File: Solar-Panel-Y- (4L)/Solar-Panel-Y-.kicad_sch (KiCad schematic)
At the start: 61 parts, among them J1 FTS-107-01-X-DV-A, J2 BM02B-SRSS-TB, SW1 D2F-L2-A1, SW2 D2F-L2-A, U1 BQ25570RGRR, U2 OPT3001, U3 MAX40200AUK

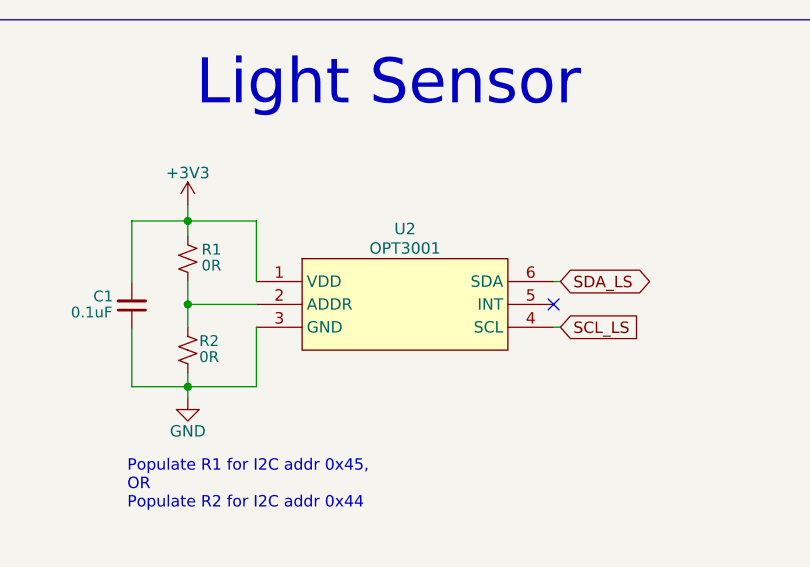
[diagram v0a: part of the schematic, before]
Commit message: Updated Sun Sensor to OPT4001
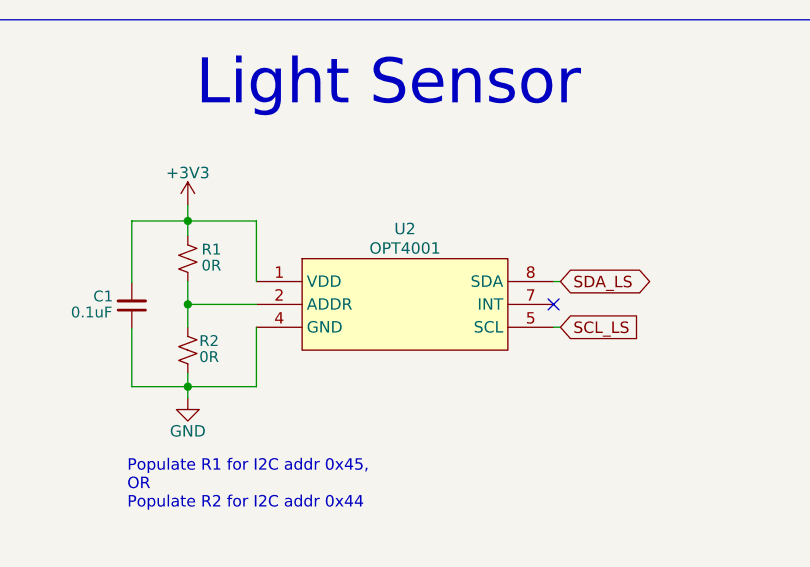
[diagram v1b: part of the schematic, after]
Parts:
- U2: value OPT3001 -> OPT4001; footprint solarpanels:OPT3001 -> Package_TO_SOT_SMD:SOT-583-8; symbol solarpanels:OPT3001 -> solarpanels:OPT4001
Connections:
- net GND: now also U2.4 (GND); no longer U2.3 (GND), U2.7 (GND)
- net SCL_LS: now also U2.5 (SCL); no longer U2.4 (SCL)
- net SDA_LS: now also U2.8 (SDA); no longer U2.6 (SDA)
- new net: U2.3 (NC), U2.6 (NC)
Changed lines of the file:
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@@
     )
   )
-  (symbol (lib_id "solarpanels:OPT3001") (at 59.817 176.657 0) (unit 1)
+  (symbol (lib_id "solarpanels:OPT4001") (at 59.817 176.657 0) (unit 1)
     (in_bom yes) (on_board yes) (dnp no)
     (property "Reference" "U2" (at 59.817 168.275 0)
       (effects (font (size 1.27 1.27)))
     )
-    (property "Value" "OPT3001" (at 59.817 170.434 0)
+    (property "Value" "OPT4001" (at 59.817 170.434 0)
       (effects (font (size 1.27 1.27)))
     )
-    (property "Footprint" "solarpanels:OPT3001" (at 59.817 183.007 0)
+    (property "Footprint" "Package_TO_SOT_SMD:SOT-583-8" (at 59.817 183.007 0)
       (effects (font (size 1.27 1.27)) hide)
     )
@@
     (pin "6")
     (pin "7")
+    (pin "8")
     (instances
       (project "Solar-Panel-Y-"
